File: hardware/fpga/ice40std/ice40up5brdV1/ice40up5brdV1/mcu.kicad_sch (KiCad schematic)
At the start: 9 parts, among them J3 Conn_01x06_Male, J4 Conn_01x04_Male, U5 ATSAMD11D14A-M

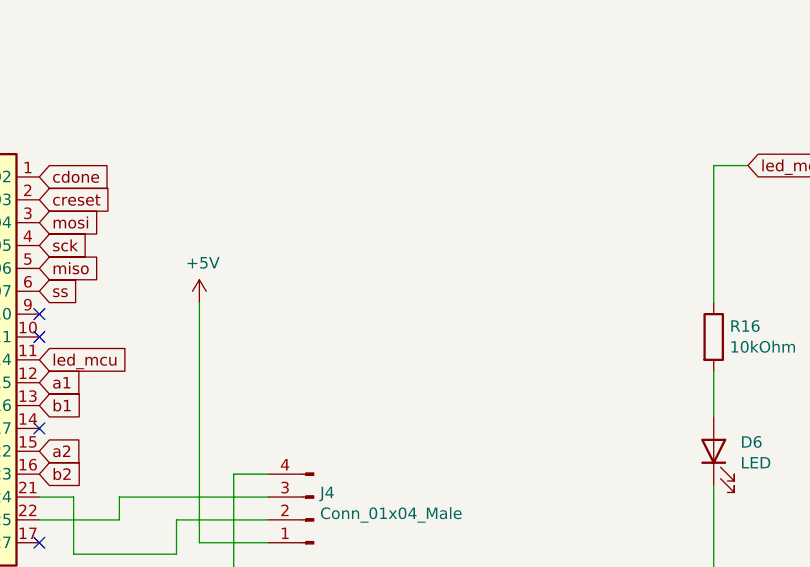
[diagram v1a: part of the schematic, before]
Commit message: started linear regs / Amphenol USB
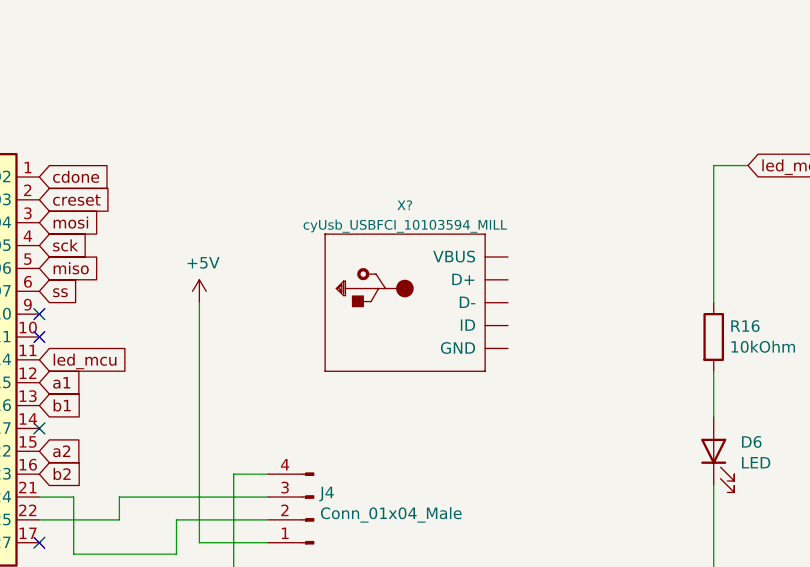
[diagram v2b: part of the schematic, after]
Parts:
- added X?: cyUsb_USBFCI_10103594_MILL, symbol conne_fci:cyUsb_USBFCI_10103594_MILL
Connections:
- new net: X?.BASE@1 (GND), X?.BASE@2 (GND), X?.GND, X?.SPRT@1 (GND), X?.SPRT@2 (GND), X?.SPRT@3 (GND), X?.SPRT@4 (GND)
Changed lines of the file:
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@@
     (pin "4")
   )
+  (symbol (lib_id "conne_fci:cyUsb_USBFCI_10103594_MILL") (at 130.81 54.61 0) (unit 1)
+    (in_bom yes) (on_board yes) (fields_autoplaced)
+    (property "Reference" "X?" (id 0) (at 129.5273 43.8262 0)
+      (effects (font (size 1.0668 1.0668)))
+    )
+    (property "Value" "cyUsb_USBFCI_10103594_MILL" (id 1) (at 129.5273 45.9979 0)
+      (effects (font (size 1.0668 1.0668)))
+    )
+    (property "Footprint" "" (id 2) (at 130.81 54.61 0)
+      (effects (font (size 1.27 1.27)) hide)
+    )
+    (property "Datasheet" "" (id 3) (at 130.81 54.61 0)
+      (effects (font (size 1.27 1.27)) hide)
+    )
+    (pin "BASE@1")
+    (pin "BASE@2")
+    (pin "D+")
+    (pin "D-")
+    (pin "GND")
+    (pin "ID")
+    (pin "SPRT@1")
+    (pin "SPRT@2")
+    (pin "SPRT@3")
+    (pin "SPRT@4")
+    (pin "VBUS")
+  )
 )

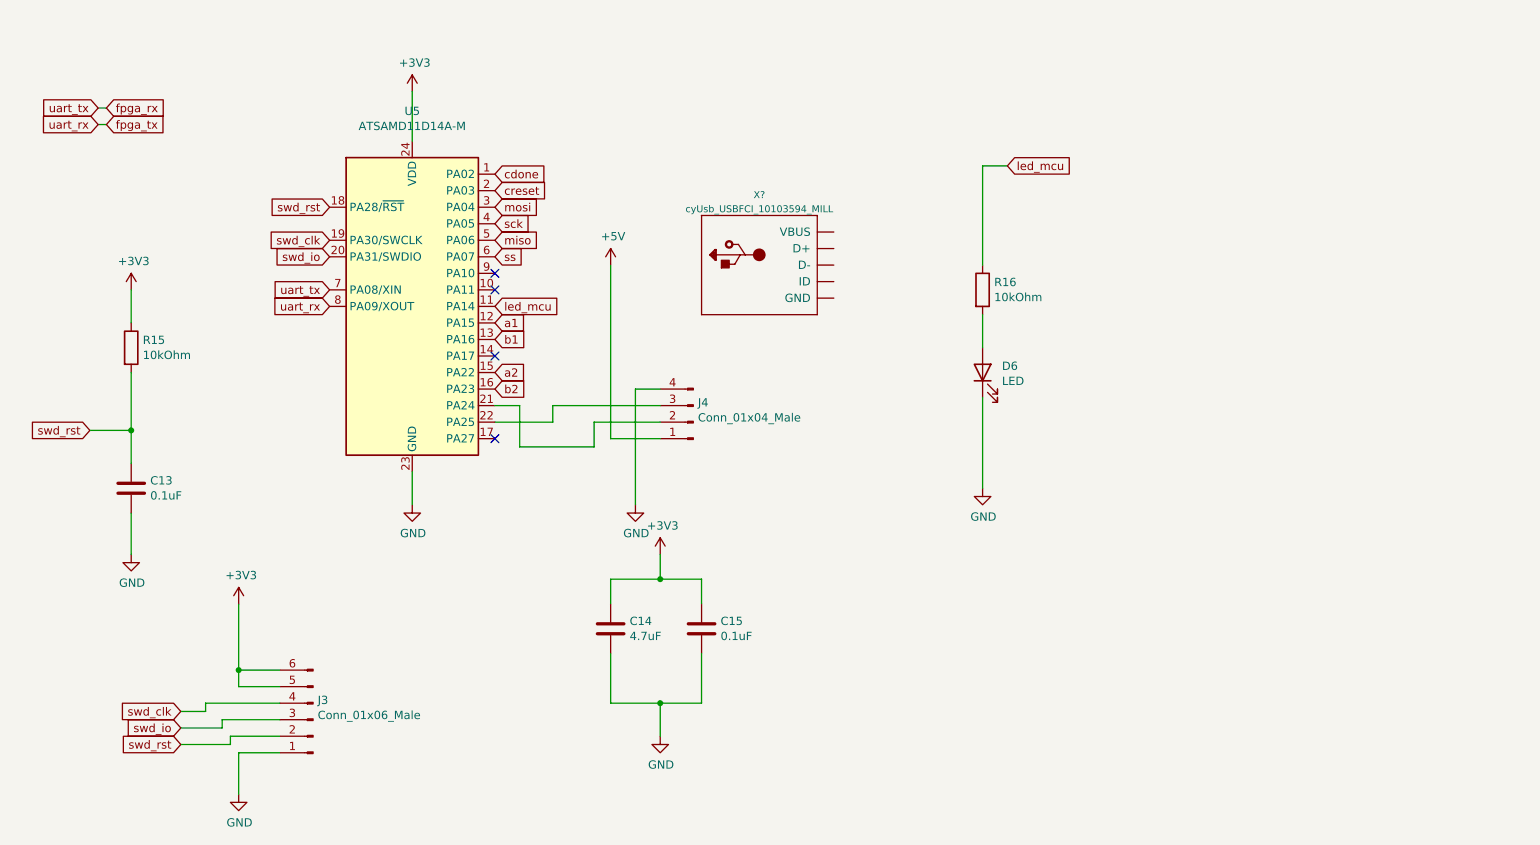
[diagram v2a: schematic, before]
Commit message: started linear regs / Amphenol USB
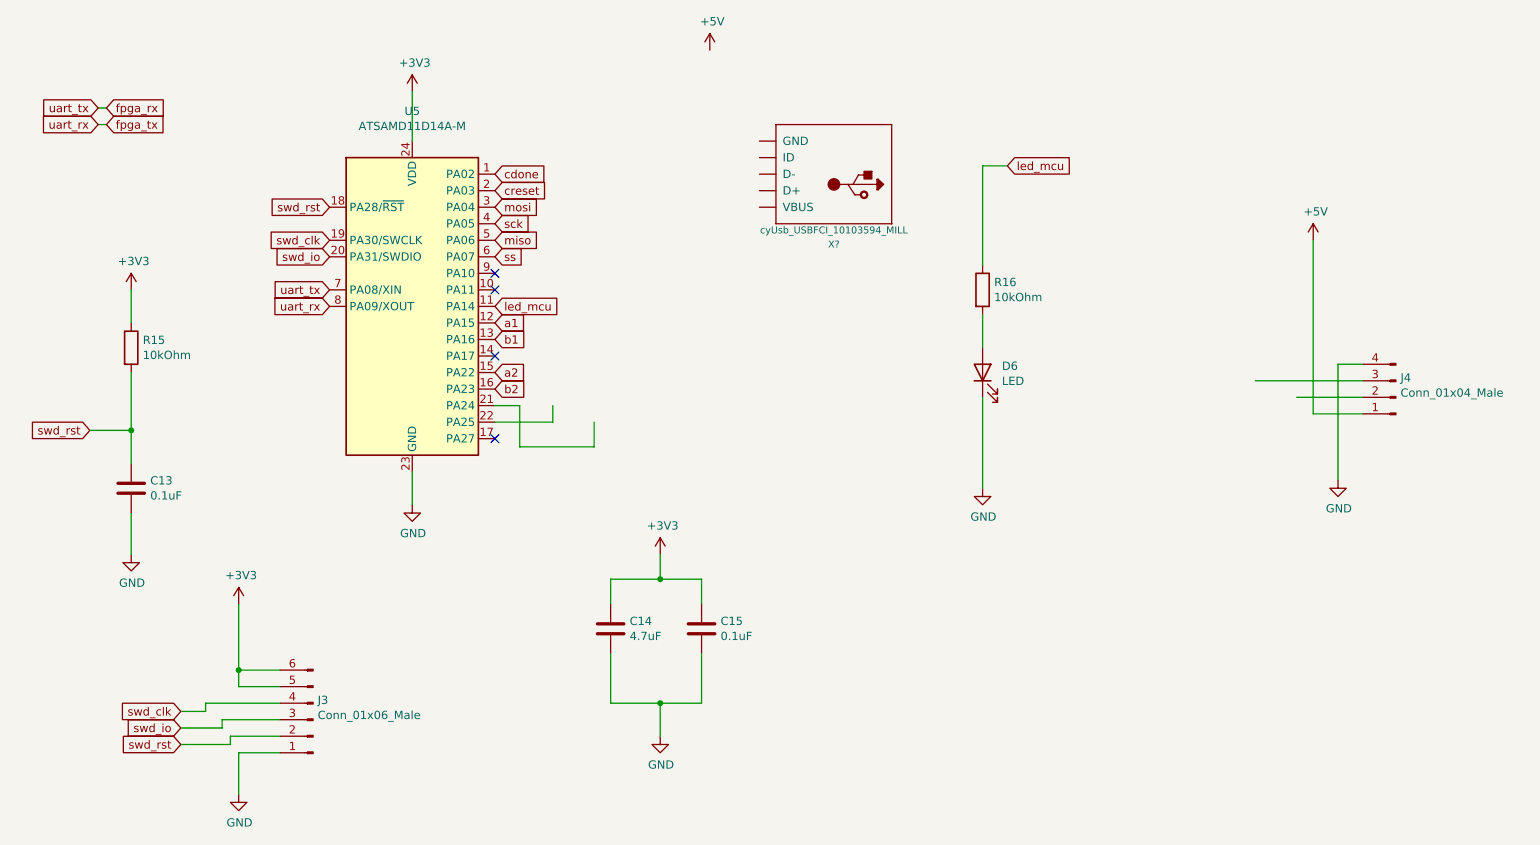
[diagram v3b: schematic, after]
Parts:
- X?: footprint (none) -> kifootp:FCI_10103594_MILL
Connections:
- net at U5.21 (PA24): no longer J4.2 (Pin_2)
- net at U5.22 (PA25): no longer J4.3 (Pin_3)
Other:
- moved on the sheet: J4, X?
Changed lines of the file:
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@@
     (stroke (width 0) (type default) (color 0 0 0 0))
   )
-  (wire (pts (xy 106.68 54.61) (xy 106.68 81.28))
+  (wire (pts (xy 214.63 50.8) (xy 214.63 77.47))
     (stroke (width 0) (type default) (color 0 0 0 0))
   )
@@
     (stroke (width 0) (type default) (color 0 0 0 0))
   )
-  (wire (pts (xy 104.14 78.74) (xy 114.3 78.74))
-    (stroke (width 0) (type default) (color 0 0 0 0))
-  )
-  (wire (pts (xy 114.3 73.66) (xy 110.49 73.66))
+  (wire (pts (xy 212.09 74.93) (xy 222.25 74.93))
+    (stroke (width 0) (type default) (color 0 0 0 0))
+  )
+  (wire (pts (xy 222.25 69.85) (xy 218.44 69.85))
     (stroke (width 0) (type default) (color 0 0 0 0))
   )
@@
     (stroke (width 0) (type default) (color 0 0 0 0))
   )
-  (wire (pts (xy 97.79 76.2) (xy 114.3 76.2))
+  (wire (pts (xy 205.74 72.39) (xy 222.25 72.39))
     (stroke (width 0) (type default) (color 0 0 0 0))
   )
@@
     (stroke (width 0) (type default) (color 0 0 0 0))
   )
-  (wire (pts (xy 110.49 73.66) (xy 110.49 91.44))
+  (wire (pts (xy 218.44 69.85) (xy 218.44 87.63))
     (stroke (width 0) (type default) (color 0 0 0 0))
   )
@@
     (stroke (width 0) (type default) (color 0 0 0 0))
   )
-  (wire (pts (xy 106.68 81.28) (xy 114.3 81.28))
+  (wire (pts (xy 214.63 77.47) (xy 222.25 77.47))
     (stroke (width 0) (type default) (color 0 0 0 0))
   )
@@
     (pin "1")
   )
-  (symbol (lib_id "power:GND") (at 110.49 91.44 0) (unit 1)
-    (in_bom yes) (on_board yes)
-    (property "Reference" "#PWR048" (id 0) (at 110.49 97.79 0)
-      (effects (font (size 1.27 1.27)) hide)
-    )
-    (property "Value" "GND" (id 1) (at 110.617 95.8342 0))
-    (property "Footprint" "" (id 2) (at 110.49 91.44 0)
-      (effects (font (size 1.27 1.27)) hide)
-    )
-    (property "Datasheet" "" (id 3) (at 110.49 91.44 0)
+  (symbol (lib_id "power:GND") (at 218.44 87.63 0) (unit 1)
+    (in_bom yes) (on_board yes)
+    (property "Reference" "#PWR048" (id 0) (at 218.44 93.98 0)
+      (effects (font (size 1.27 1.27)) hide)
+    )
+    (property "Value" "GND" (id 1) (at 218.567 92.0242 0))
+    (property "Footprint" "" (id 2) (at 218.44 87.63 0)
+      (effects (font (size 1.27 1.27)) hide)
+    )
+    (property "Datasheet" "" (id 3) (at 218.44 87.63 0)
       (effects (font (size 1.27 1.27)) hide)
     )
@@
     (pin "1")
   )
-  (symbol (lib_id "power:+5V") (at 106.68 54.61 0) (unit 1)
-    (in_bom yes) (on_board yes)
-    (property "Reference" "#PWR047" (id 0) (at 106.68 58.42 0)
-      (effects (font (size 1.27 1.27)) hide)
-    )
-    (property "Value" "+5V" (id 1) (at 107.061 50.2158 0))
-    (property "Footprint" "" (id 2) (at 106.68 54.61 0)
-      (effects (font (size 1.27 1.27)) hide)
-    )
-    (property "Datasheet" "" (id 3) (at 106.68 54.61 0)
+  (symbol (lib_id "power:+5V") (at 214.63 50.8 0) (unit 1)
+    (in_bom yes) (on_board yes)
+    (property "Reference" "#PWR047" (id 0) (at 214.63 54.61 0)
+      (effects (font (size 1.27 1.27)) hide)
+    )
+    (property "Value" "+5V" (id 1) (at 215.011 46.4058 0))
+    (property "Footprint" "" (id 2) (at 214.63 50.8 0)
+      (effects (font (size 1.27 1.27)) hide)
+    )
+    (property "Datasheet" "" (id 3) (at 214.63 50.8 0)
       (effects (font (size 1.27 1.27)) hide)
     )
@@
     (pin "1")
   )
-  (symbol (lib_id "Connector:Conn_01x04_Male") (at 119.38 78.74 180) (unit 1)
-    (in_bom yes) (on_board yes)
-    (property "Reference" "J4" (id 0) (at 120.0912 75.7428 0)
+  (symbol (lib_id "Connector:Conn_01x04_Male") (at 227.33 74.93 180) (unit 1)
+    (in_bom yes) (on_board yes)
+    (property "Reference" "J4" (id 0) (at 228.0412 71.9328 0)
       (effects (font (size 1.27 1.27)) (justify right))
     )
-    (property "Value" "Conn_01x04_Male" (id 1) (at 120.0912 78.0542 0)
+    (property "Value" "Conn_01x04_Male" (id 1) (at 228.0412 74.2442 0)
       (effects (font (size 1.27 1.27)) (justify right))
     )
-    (property "Footprint" "Connector_PinHeader_2.54mm:PinHeader_1x04_P2.54mm_Horizontal" (id 2) (at 119.38 78.74 0)
-      (effects (font (size 1.27 1.27)) hide)
-    )
-    (property "Datasheet" "~" (id 3) (at 119.38 78.74 0)
+    (property "Footprint" "Connector_PinHeader_2.54mm:PinHeader_1x04_P2.54mm_Horizontal" (id 2) (at 227.33 74.93 0)
+      (effects (font (size 1.27 1.27)) hide)
+    )
+    (property "Datasheet" "~" (id 3) (at 227.33 74.93 0)
       (effects (font (size 1.27 1.27)) hide)
     )
@@
     (pin "4")
   )
-  (symbol (lib_id "conne_fci:cyUsb_USBFCI_10103594_MILL") (at 130.81 54.61 0) (unit 1)
+  (symbol (lib_id "power:+5V") (at 121.92 21.59 0) (unit 1)
+    (in_bom yes) (on_board yes)
+    (property "Reference" "#PWR?" (id 0) (at 121.92 25.4 0)
+      (effects (font (size 1.27 1.27)) hide)
+    )
+    (property "Value" "+5V" (id 1) (at 122.301 17.1958 0))
+    (property "Footprint" "" (id 2) (at 121.92 21.59 0)
+      (effects (font (size 1.27 1.27)) hide)
+    )
+    (property "Datasheet" "" (id 3) (at 121.92 21.59 0)
+      (effects (font (size 1.27 1.27)) hide)
+    )
+    (pin "1")
+  )
+  (symbol (lib_id "conne_fci:cyUsb_USBFCI_10103594_MILL") (at 139.7 40.64 180) (unit 1)
     (in_bom yes) (on_board yes) (fields_autoplaced)
-    (property "Reference" "X?" (id 0) (at 129.5273 43.8262 0)
+    (property "Reference" "X?" (id 0) (at 140.9827 51.4238 0)
       (effects (font (size 1.0668 1.0668)))
     )
-    (property "Value" "cyUsb_USBFCI_10103594_MILL" (id 1) (at 129.5273 45.9979 0)
+    (property "Value" "cyUsb_USBFCI_10103594_MILL" (id 1) (at 140.9827 49.2521 0)
       (effects (font (size 1.0668 1.0668)))
     )
-    (property "Footprint" "" (id 2) (at 130.81 54.61 0)
-      (effects (font (size 1.27 1.27)) hide)
-    )
-    (property "Datasheet" "" (id 3) (at 130.81 54.61 0)
-      (effects (font (size 1.27 1.27)) hide)
-    )
+    (property "Footprint" "kifootp:FCI_10103594_MILL" (id 2) (at 139.7 40.64 0)
+      (effects (font (size 1.27 1.27)) hide)
+    )
+    (property "Datasheet" "" (id 3) (at 139.7 40.64 0)
+      (effects (font (size 1.27 1.27)) hide)
+    )
